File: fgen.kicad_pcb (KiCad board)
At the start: 2 copper layers, 18 parts, among them J1 AudioPlug3, J2 Conn_01x02_Female, Q1 TIP29C, Q2 TIP30C, Q3 2N3904, Q4 2N3906, T1 Transformer_1P_1S, U1 LM741

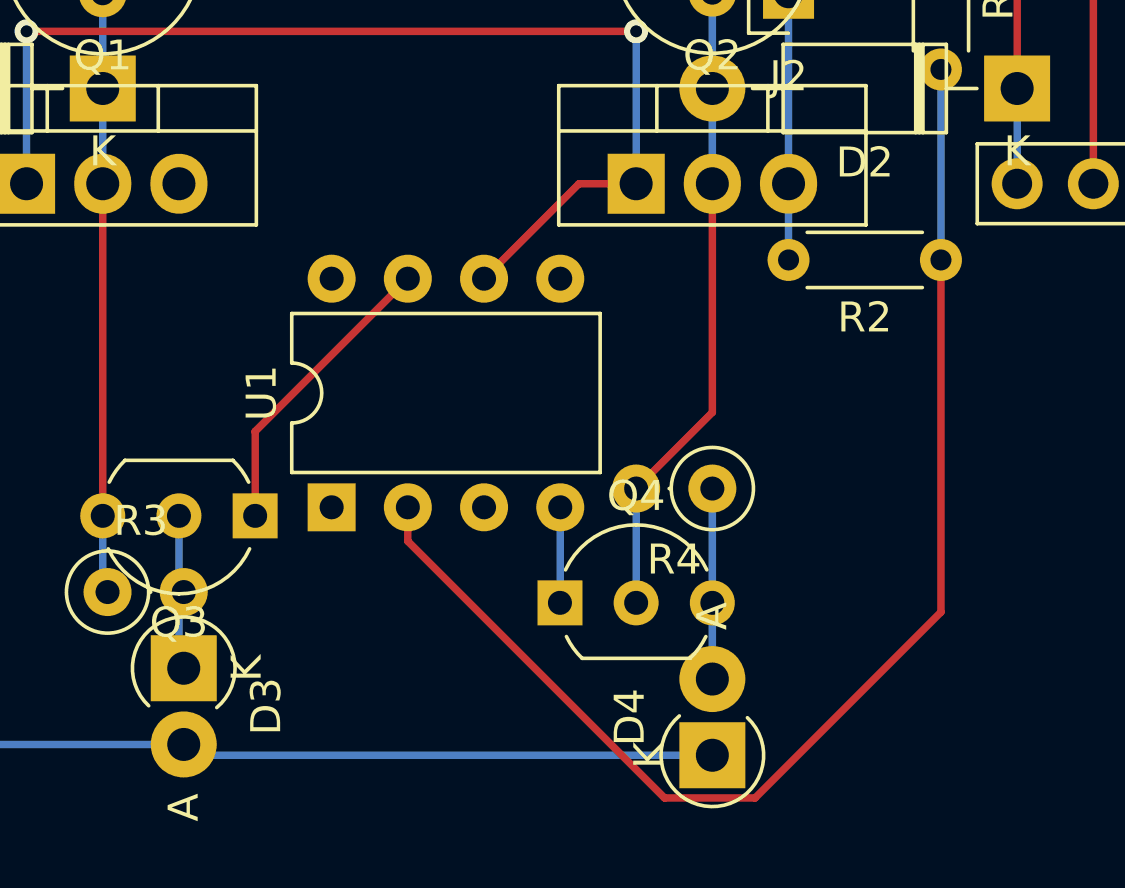
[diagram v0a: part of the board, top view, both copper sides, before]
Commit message: schematic bug fix
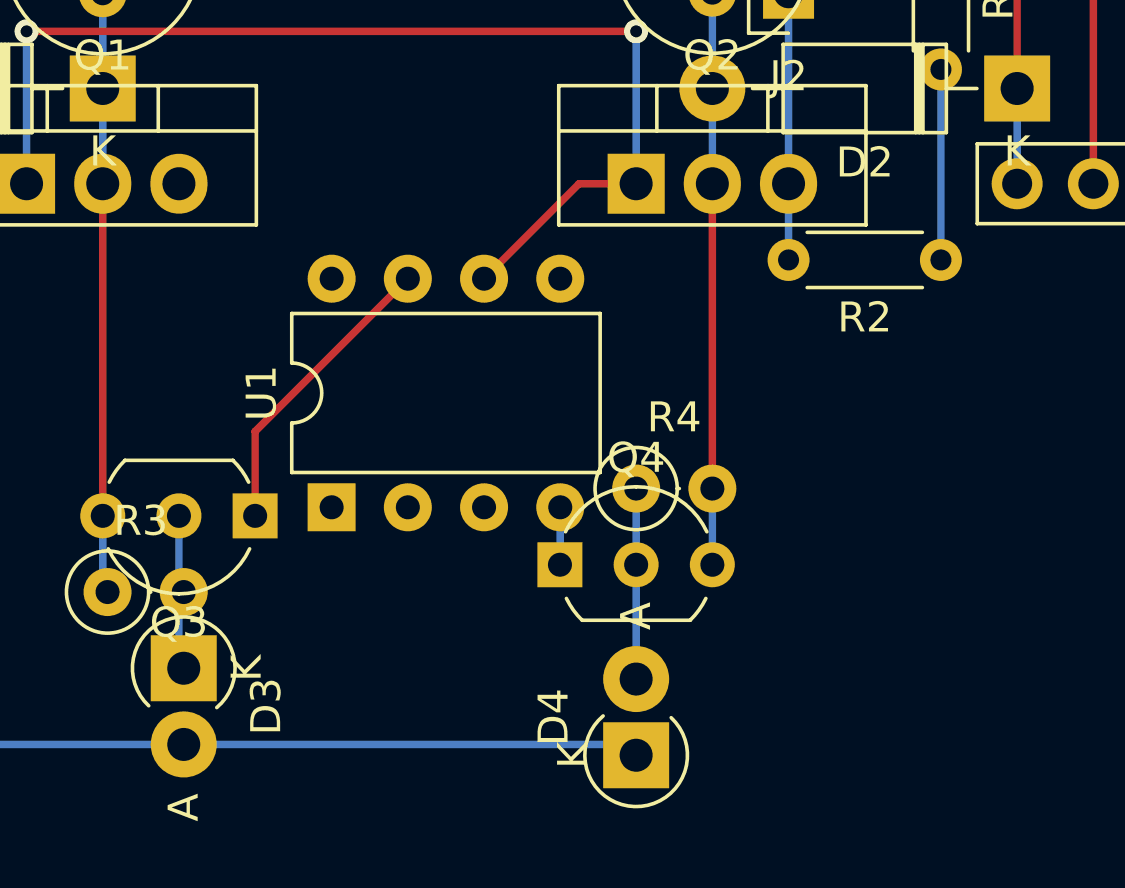
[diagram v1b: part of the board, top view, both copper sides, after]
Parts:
- R1: value 22k -> 1k
- R2: value 180k -> 100k
- moved D4 2.54 mm to (66.0, 108.0)
- moved R4 2.54 mm to (66.0, 99.1), turned to 0 degrees
- moved Q4 1.27 mm to (63.5, 101.6)
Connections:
- Q4 pad 2: -VDC -> Net-(D4-Pad2)
- Q4 pad 3: Net-(D4-Pad2) -> -VDC
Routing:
- net Net-(R1-Pad2): track 43.1 -> 6.35 mm
- net GND: track 132.6 -> 130.1 mm
- net -VDC: track 21.4 -> 19.1 mm
- net -15V: track 3.19 -> 1.92 mm
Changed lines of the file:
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@@
       (effects (font (size 1 1) (thickness 0.15)))
     )
-    (fp_text value "180k" (at 2.54 1.92) (layer "F.Fab")
+    (fp_text value "100k" (at 2.54 1.92) (layer "F.Fab")
       (effects (font (size 1 1) (thickness 0.15)))
     )
@@
       (effects (font (size 1 1) (thickness 0.15)))
     )
-    (fp_text value "22k" (at 2.54 1.92 90) (layer "F.Fab")
+    (fp_text value "1k" (at 2.54 1.92 90) (layer "F.Fab")
       (effects (font (size 1 1) (thickness 0.15)))
     )
@@
   )
   (footprint "Resistor_THT:R_Axial_DIN0207_L6.3mm_D2.5mm_P2.54mm_Vertical" (layer "F.Cu")
-    (at 68.58 99.06 180)
+    (at 66.04 99.06)
     (descr "Resistor, Axial_DIN0207 series, Axial, Vertical, pin pitch=2.54mm, 0.25W = 1/4W, length*diameter=6.3*2.5mm^2, http://cdn-reichelt.de/documents/datenblatt/B400/1_4W%23YAG.pdf")
     (tags "Resistor Axial_DIN0207 series Axial Vertical pin pitch 2.54mm 0.25W = 1/4W length 6.3mm diameter 2.5mm")
@@
     (fp_line (start 0 0) (end 2.54 0) (layer "F.Fab") (width 0.1))
     (fp_circle (center 0 0) (end 1.25 0) (layer "F.Fab") (width 0.1) (fill none))
-    (pad "1" thru_hole circle (at 0 0 180) (size 1.6 1.6) (drill 0.8) (layers *.Cu *.Mask)
+    (pad "1" thru_hole circle (at 0 0) (size 1.6 1.6) (drill 0.8) (layers *.Cu *.Mask)
       (net 6 "Net-(D4-Pad2)") (pintype "passive"))
-    (pad "2" thru_hole oval (at 2.54 0 180) (size 1.6 1.6) (drill 0.8) (layers *.Cu *.Mask)
+    (pad "2" thru_hole oval (at 2.54 0) (size 1.6 1.6) (drill 0.8) (layers *.Cu *.Mask)
       (net 3 "-VDC") (pintype "passive"))
     (model "${KICAD6_3DMODEL_DIR}/Resistor_THT.3dshapes/R_Axial_DIN0207_L6.3mm_D2.5mm_P2.54mm_Vertical.wrl"
@@
   )
   (footprint "Diode_THT:D_DO-41_SOD81_P2.54mm_Vertical_AnodeUp" (layer "F.Cu")
-    (at 68.58 107.95 90)
+    (at 66.04 107.95 90)
     (descr "Diode, DO-41_SOD81 series, Axial, Vertical, pin pitch=2.54mm, , length*diameter=5.2*2.7mm^2, , http://www.diodes.com/_files/packages/DO-41%20(Plastic).pdf")
     (tags "Diode DO-41_SOD81 series Axial Vertical pin pitch 2.54mm  length 5.2mm diameter 2.7mm")
@@
   )
   (footprint "Package_TO_SOT_THT:TO-92_Inline_Wide" (layer "F.Cu")
-    (at 63.5 102.87)
+    (at 63.5 101.6)
     (descr "TO-92 leads in-line, wide, drill 0.75mm (see NXP sot054_po.pdf)")
     (tags "to-92 sc-43 sc-43a sot54 PA33 transistor")
@@
       (net 10 "-15V") (pinfunction "E") (pintype "passive"))
     (pad "2" thru_hole circle (at 2.54 0) (size 1.5 1.5) (drill 0.8) (layers *.Cu *.Mask)
-      (net 3 "-VDC") (pinfunction "B") (pintype "input"))
+      (net 6 "Net-(D4-Pad2)") (pinfunction "B") (pintype "input"))
     (pad "3" thru_hole circle (at 5.08 0) (size 1.5 1.5) (drill 0.8) (layers *.Cu *.Mask)
-      (net 6 "Net-(D4-Pad2)") (pinfunction "C") (pintype "passive"))
+      (net 3 "-VDC") (pinfunction "C") (pintype "passive"))
     (model "${KICAD6_3DMODEL_DIR}/Package_TO_SOT_THT.3dshapes/TO-92_Inline_Wide.wrl"
       (offset (xyz 0 0 0))
@@
   (segment (start 81.28 80.01) (end 81.28 88.9) (width 0.25) (layer "F.Cu") (net 2))
   (via (at 81.28 80.01) (size 0.8) (drill 0.4) (layers "F.Cu" "B.Cu") (net 2))
-  (segment (start 50.96 107.59) (end 51.32 107.95) (width 0.25) (layer "B.Cu") (net 2))
   (segment (start 81.28 80.01) (end 76.2 80.01) (width 0.25) (layer "B.Cu") (net 2))
   (segment (start 26.67 106.68) (end 26.67 80.01) (width 0.25) (layer "B.Cu") (net 2))
-  (segment (start 51.32 107.95) (end 68.58 107.95) (width 0.25) (layer "B.Cu") (net 2))
+  (segment (start 65.68 107.59) (end 66.04 107.95) (width 0.25) (layer "B.Cu") (net 2))
+  (segment (start 50.96 107.59) (end 65.68 107.59) (width 0.25) (layer "B.Cu") (net 2))
   (segment (start 27.58 107.59) (end 26.67 106.68) (width 0.25) (layer "B.Cu") (net 2))
   (segment (start 26.67 80.01) (end 71.12 80.01) (width 0.25) (layer "B.Cu") (net 2))
   (segment (start 76.2 80.01) (end 71.12 80.01) (width 0.25) (layer "B.Cu") (net 2))
   (segment (start 50.96 107.59) (end 27.58 107.59) (width 0.25) (layer "B.Cu") (net 2))
-  (segment (start 68.58 88.9) (end 68.58 96.52) (width 0.25) (layer "F.Cu") (net 3))
-  (segment (start 68.58 96.52) (end 66.04 99.06) (width 0.25) (layer "F.Cu") (net 3))
-  (segment (start 66.04 102.87) (end 66.04 99.06) (width 0.25) (layer "B.Cu") (net 3))
+  (segment (start 68.58 99.06) (end 68.58 88.9) (width 0.25) (layer "F.Cu") (net 3))
   (segment (start 68.58 82.53) (end 68.58 88.9) (width 0.25) (layer "B.Cu") (net 3))
+  (segment (start 68.58 101.6) (end 68.58 99.06) (width 0.25) (layer "B.Cu") (net 3))
   (segment (start 38.1 77.47) (end 38.1 85.725) (width 0.25) (layer "F.Cu") (net 4))
   (segment (start 78.74 85.725) (end 78.74 76.2) (width 0.25) (layer "F.Cu") (net 4))
@@
   (segment (start 50.8 104.89) (end 50.96 105.05) (width 0.25) (layer "B.Cu") (net 5))
   (segment (start 50.8 99.97) (end 50.8 104.89) (width 0.25) (layer "B.Cu") (net 5))
-  (segment (start 68.58 99.06) (end 68.58 105.41) (width 0.25) (layer "B.Cu") (net 6))
+  (segment (start 66.04 99.06) (end 66.04 105.41) (width 0.25) (layer "B.Cu") (net 6))
   (segment (start 71.12 88.9) (end 71.12 91.44) (width 0.25) (layer "B.Cu") (net 7))
   (segment (start 71.12 82.55) (end 71.12 88.9) (width 0.25) (layer "B.Cu") (net 7))
@@
   (segment (start 53.34 97.155) (end 58.43 92.065) (width 0.25) (layer "F.Cu") (net 9))
   (segment (start 53.34 99.97) (end 53.34 97.155) (width 0.25) (layer "F.Cu") (net 9))
-  (segment (start 63.51 99.685) (end 63.51 102.86) (width 0.25) (layer "B.Cu") (net 10))
-  (segment (start 63.51 102.86) (end 63.5 102.87) (width 0.25) (layer "B.Cu") (net 10))
-  (segment (start 70.004511 109.374511) (end 76.2 103.179022) (width 0.25) (layer "F.Cu") (net 11))
-  (segment (start 58.43 100.81637) (end 66.988141 109.374511) (width 0.25) (layer "F.Cu") (net 11))
-  (segment (start 58.43 99.685) (end 58.43 100.81637) (width 0.25) (layer "F.Cu") (net 11))
-  (segment (start 76.2 103.179022) (end 76.2 91.44) (width 0.25) (layer "F.Cu") (net 11))
-  (segment (start 66.988141 109.374511) (end 70.004511 109.374511) (width 0.25) (layer "F.Cu") (net 11))
+  (segment (start 63.51 101.59) (end 63.5 101.6) (width 0.25) (layer "B.Cu") (net 10))
+  (segment (start 63.51 99.685) (end 63.51 101.59) (width 0.25) (layer "B.Cu") (net 10))
   (segment (start 76.2 85.09) (end 76.2 91.44) (width 0.25) (layer "B.Cu") (net 11))
 )

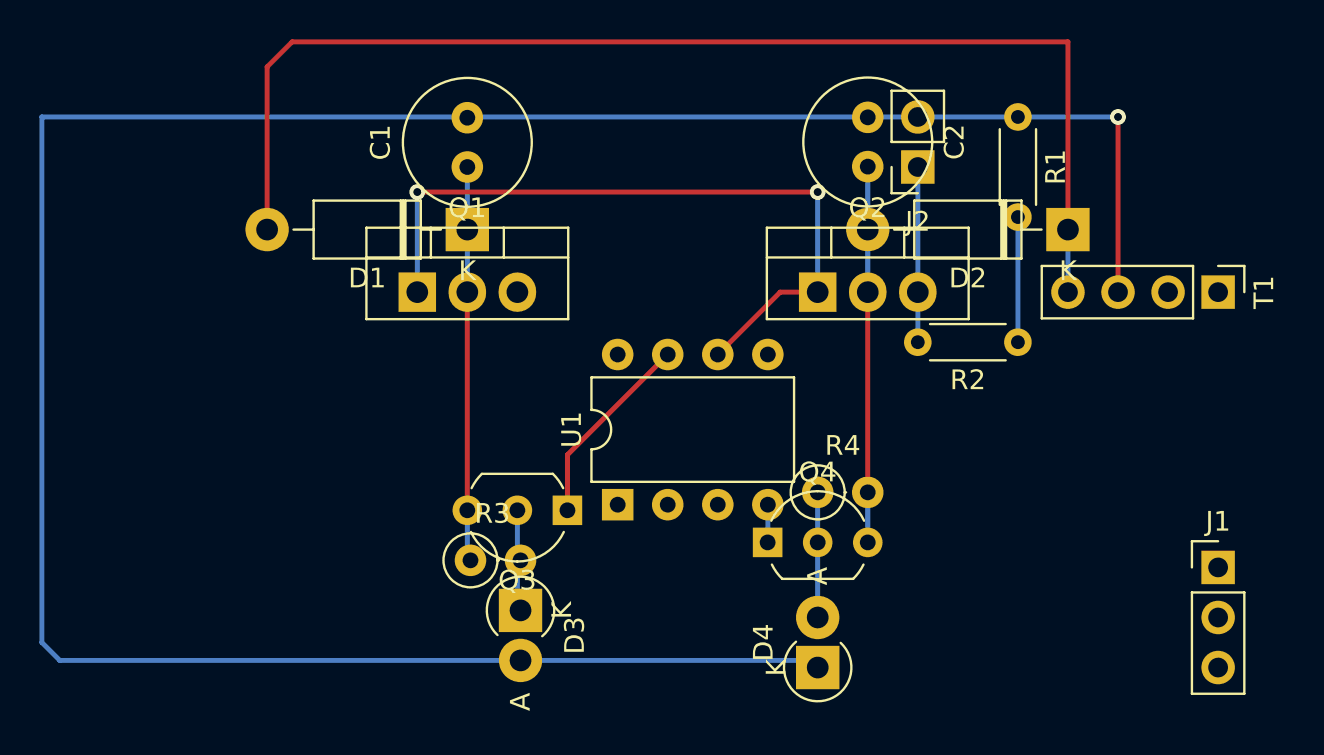
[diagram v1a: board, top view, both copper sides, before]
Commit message: Prototyped on breadboard, updated gain resistor
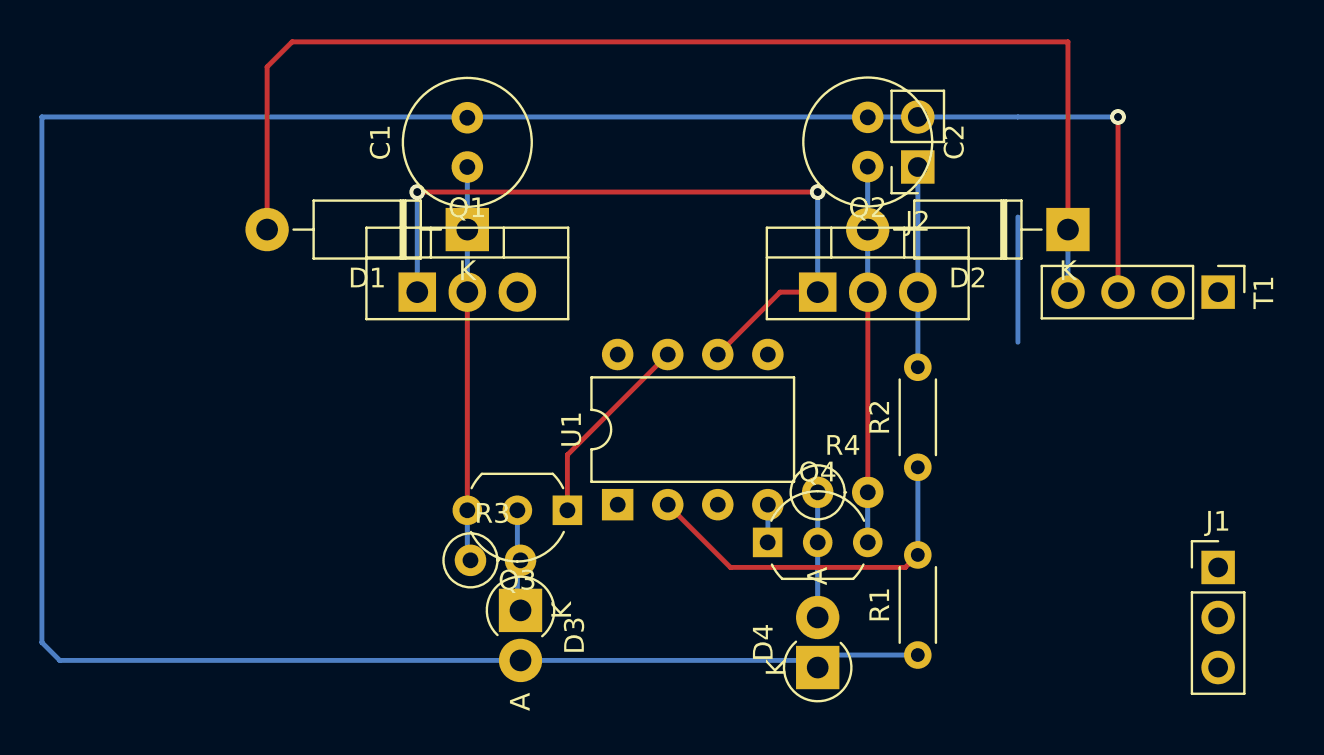
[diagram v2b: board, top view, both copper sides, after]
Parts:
- R1: value 1k -> 470
- moved R1 27.8 mm to (71.1, 107.3), turned to 90 degrees
- moved R2 8.13 mm to (71.1, 97.8), turned to 90 degrees
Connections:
- net Net-(Q1-Pad1) renamed /ctrl
- net Net-(R1-Pad2) renamed /fb
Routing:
- net /fb: track 6.35 -> 18.7 mm
- net (no net): track 0.00 -> 6.35 mm
- net GND: track 130.1 -> 135.4 mm
- net /Vout: track 8.89 -> 10.2 mm
